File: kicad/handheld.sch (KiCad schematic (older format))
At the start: 30 parts, among them J1 Conn_01x08, J2 61300311121, J3 AVR-PDI-6, SW1 HOLD, SW10 SELECT, SW2 PAUSE, SW3 SDROP, SW4 HDROP, SW5 ROTR, SW6 RIGHT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

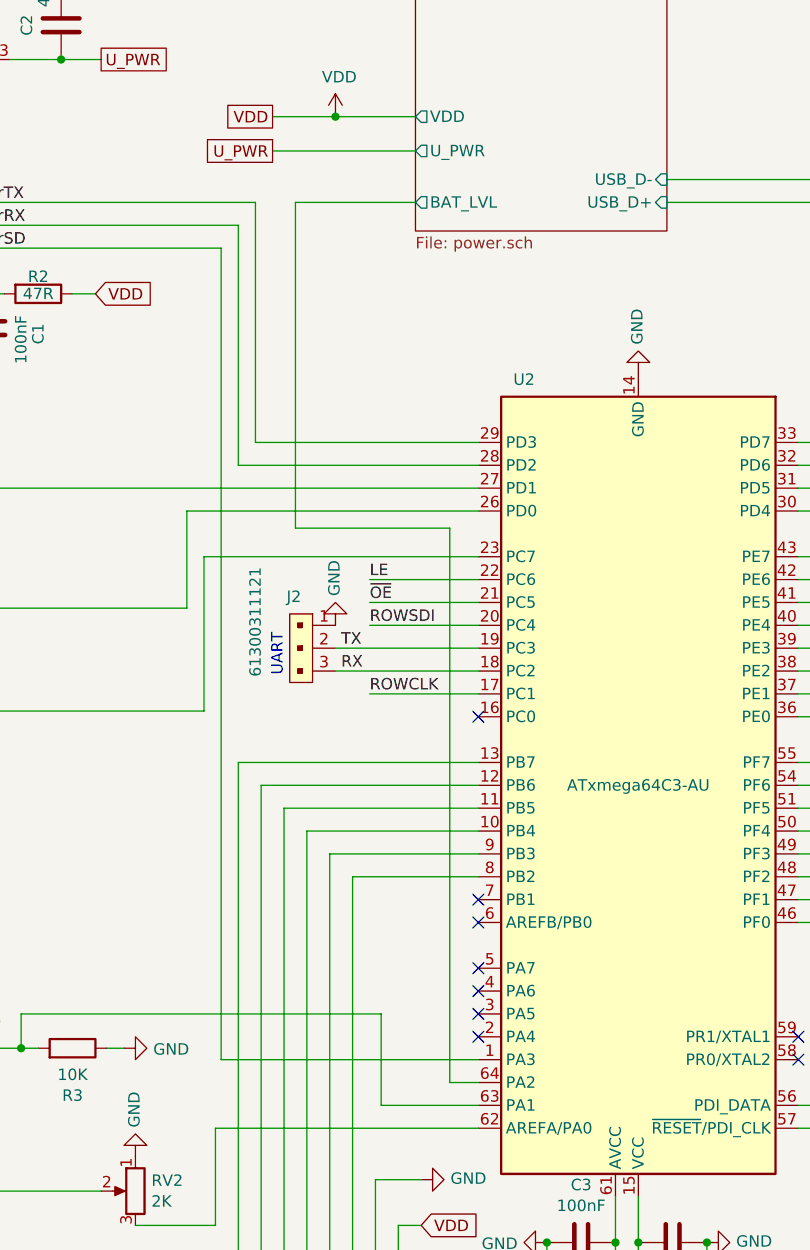
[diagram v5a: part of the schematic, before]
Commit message: Wired up battery level check
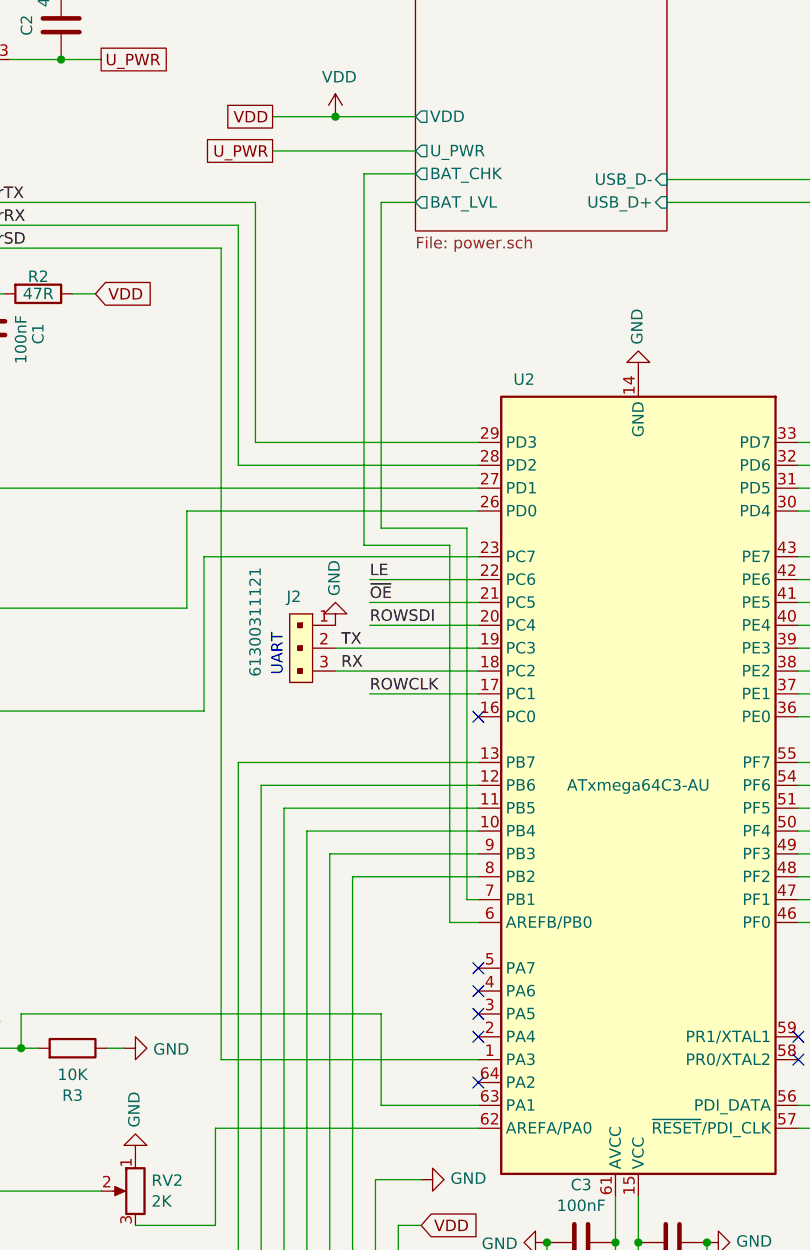
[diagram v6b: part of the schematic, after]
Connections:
- net power/BAT_LVL: now also U2.7 (PB1); no longer U2.64 (PA2)
- net power/BAT_CHK: now reaches U2.6 (AREFB/PB0)
- no-connect marks 9 -> 8
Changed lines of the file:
@@
 F5 "USB_D-" I R 4575 2025 50
 F6 "USB_D+" I R 4575 2125 50
+F7 "BAT_CHK" O L 3475 2000 50
 $EndSheet
 Wire Wire Line
-	3475 2125 2950 2125
-Wire Wire Line
-	3625 5975 3750 5975
+	3475 2125 3325 2125
 Text GLabel 2850 1750 0    50   UnSpc ~ 0
 VDD
@@
 	1925 1500 2100 1500
 Wire Wire Line
-	3625 3550 3625 5975
-Wire Wire Line
-	2950 2125 2950 3550
-Wire Wire Line
-	2950 3550 3625 3550
+	3700 3550 3700 5175
+Wire Wire Line
+	3325 2125 3325 3550
+Wire Wire Line
+	3325 3550 3700 3550
 Text Notes 2750 7075 0    50   ~ 0
 GPIO Expansion
@@
 	1125 4350 2550 4350
 Connection ~ 625  4350
-NoConn ~ 3750 5275
 Wire Wire Line
 	1750 5675 3325 5675
@@
 Wire Wire Line
 	3200 5075 3200 6725
-NoConn ~ 3750 5175
 Wire Wire Line
 	4350 6675 4350 7075
@@
 Wire Wire Line
 	5550 3375 5150 3375
+Wire Wire Line
+	3700 5175 3750 5175
+NoConn ~ 3750 5975
+Wire Wire Line
+	3475 2000 3250 2000
+Wire Wire Line
+	3250 2000 3250 3625
+Wire Wire Line
+	3250 3625 3625 3625
+Wire Wire Line
+	3625 3625 3625 5275
+Wire Wire Line
+	3625 5275 3750 5275
 Wire Bus Line
 	5775 4875 5775 5175

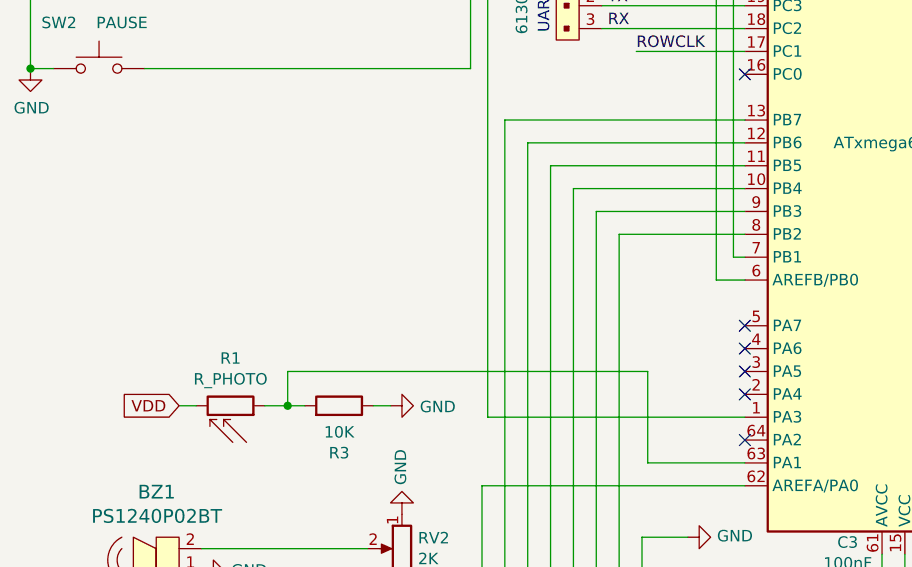
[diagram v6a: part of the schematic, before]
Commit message: Fix register footprints and add batt indicator
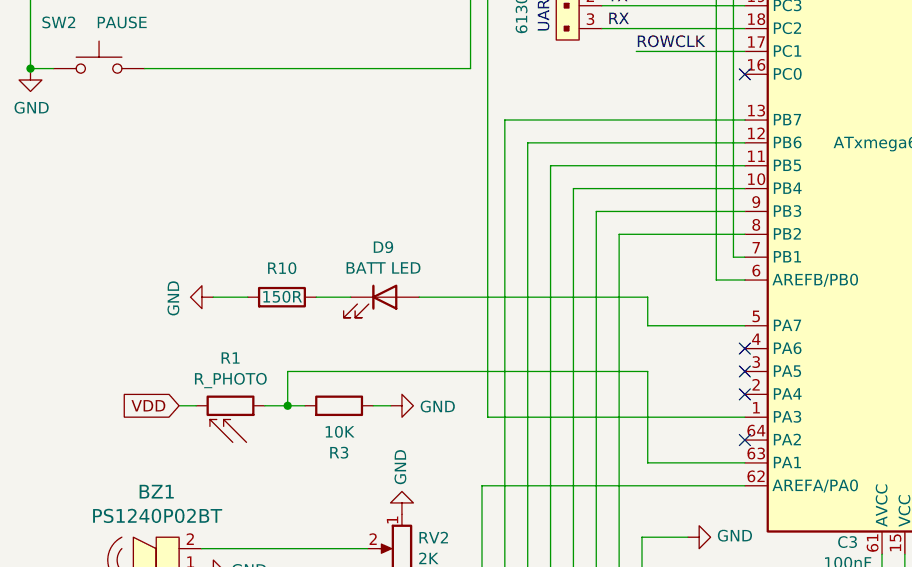
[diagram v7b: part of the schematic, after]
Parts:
- added D9: BATT LED, LED_THT:LED_D3.0mm, symbol Device:LED
- added R10: 150R, Resistor_SMD:R_0805_2012Metric_Pad1.15x1.40mm_HandSolder, symbol Device:R
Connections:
- net GND: now also R10.2
- net at U2.5 (PA7): now also D9.2 (A)
- new net: D9.1 (K), R10.1
- no-connect marks 8 -> 7
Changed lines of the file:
@@
 IrSD
 NoConn ~ 3750 4375
-NoConn ~ 3750 5475
 NoConn ~ 3750 5575
 NoConn ~ 3750 5675
@@
 Wire Wire Line
 	3625 5275 3750 5275
+$Comp
+L Device:LED D9
+U 1 1 5FE05E08
+P 2175 5350
+F 0 "D9" H 2168 5567 50  0000 C CNN
+F 1 "BATT LED" H 2168 5476 50  0000 C CNN
+F 2 "LED_THT:LED_D3.0mm" H 2175 5350 50  0001 C CNN
+F 3 "~" H 2175 5350 50  0001 C CNN
+	1    2175 5350
+	1    0    0    -1
+$EndComp
+Wire Wire Line
+	2325 5350 3325 5350
+Wire Wire Line
+	3325 5350 3325 5475
+Wire Wire Line
+	3325 5475 3750 5475
+$Comp
+L Device:R R10
+U 1 1 5FE0E9B8
+P 1725 5350
+F 0 "R10" V 1850 5350 50  0000 C CNN
+F 1 "150R" V 1725 5350 50  0000 C CNN
+F 2 "Resistor_SMD:R_0805_2012Metric_Pad1.15x1.40mm_HandSolder" V 1655 5350 50  0001 C CNN
+F 3 "~" H 1725 5350 50  0001 C CNN
+	1    1725 5350
+	0    1    -1   0
+$EndComp
+Wire Wire Line
+	1875 5350 2025 5350
+$Comp
+L power:GND #PWR0102
+U 1 1 5FE1738F
+P 1425 5350
+F 0 "#PWR0102" H 1425 5100 50  0001 C CNN
+F 1 "GND" H 1430 5177 50  0000 C CNN
+F 2 "" H 1425 5350 50  0001 C CNN
+F 3 "" H 1425 5350 50  0001 C CNN
+	1    1425 5350
+	0    1    1    0
+$EndComp
+Wire Wire Line
+	1425 5350 1575 5350
 Wire Bus Line
 	5775 4875 5775 5175

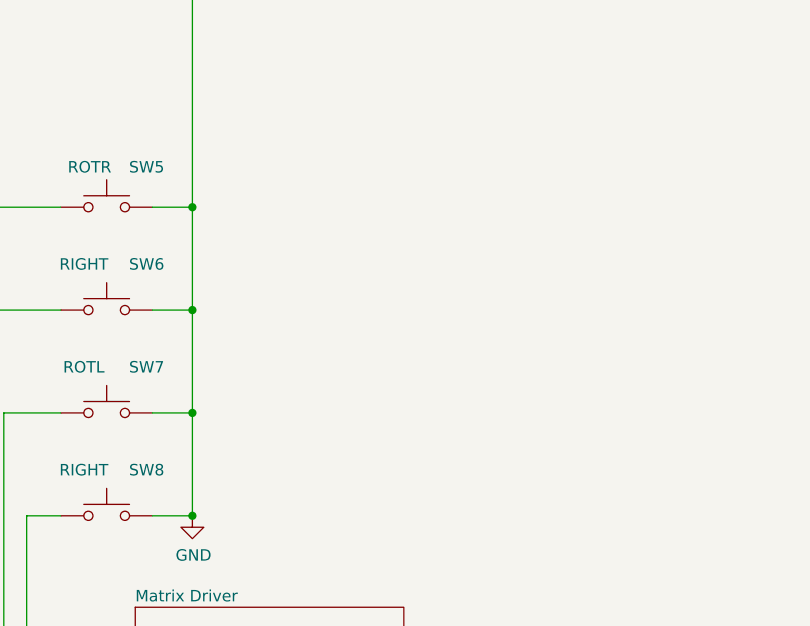
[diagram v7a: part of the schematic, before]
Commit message: Switched to registers with clear
Also added the mountng holes as annotated symbols with footprints.
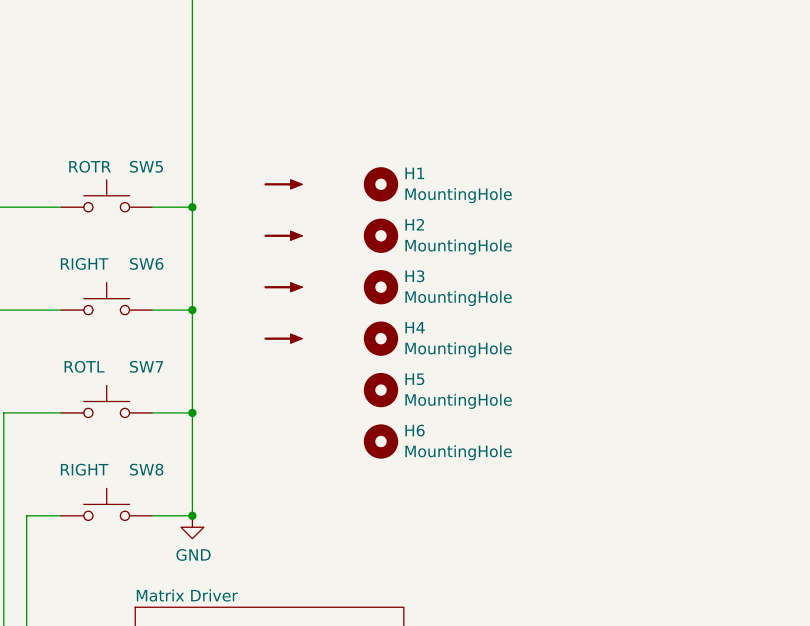
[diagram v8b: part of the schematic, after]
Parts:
- added H1, H2, H3, H4, H5, H6: MountingHole, MountingHole:MountingHole_3.2mm_M3, symbol Mechanical:MountingHole
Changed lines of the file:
@@
 Wire Bus Line
 	5775 4475 5775 4875
+$Comp
+L Mechanical:MountingHole H1
+U 1 1 5FE0E6C0
+P 8625 2000
+F 0 "H1" H 8725 2046 50  0000 L CNN
+F 1 "MountingHole" H 8725 1955 50  0000 L CNN
+F 2 "MountingHole:MountingHole_3.2mm_M3" H 8625 2000 50  0001 C CNN
+F 3 "~" H 8625 2000 50  0001 C CNN
+	1    8625 2000
+	1    0    0    -1
+$EndComp
+$Comp
+L Mechanical:MountingHole H2
+U 1 1 5FE0E95C
+P 8625 2225
+F 0 "H2" H 8725 2271 50  0000 L CNN
+F 1 "MountingHole" H 8725 2180 50  0000 L CNN
+F 2 "MountingHole:MountingHole_3.2mm_M3" H 8625 2225 50  0001 C CNN
+F 3 "~" H 8625 2225 50  0001 C CNN
+	1    8625 2225
+	1    0    0    -1
+$EndComp
+$Comp
+L Mechanical:MountingHole H3
+U 1 1 5FE0F471
+P 8625 2450
+F 0 "H3" H 8725 2496 50  0000 L CNN
+F 1 "MountingHole" H 8725 2405 50  0000 L CNN
+F 2 "MountingHole:MountingHole_3.2mm_M3" H 8625 2450 50  0001 C CNN
+F 3 "~" H 8625 2450 50  0001 C CNN
+	1    8625 2450
+	1    0    0    -1
+$EndComp
+$Comp
+L Mechanical:MountingHole H4
+U 1 1 5FE0F840
+P 8625 2675
+F 0 "H4" H 8725 2721 50  0000 L CNN
+F 1 "MountingHole" H 8725 2630 50  0000 L CNN
+F 2 "MountingHole:MountingHole_3.2mm_M3" H 8625 2675 50  0001 C CNN
+F 3 "~" H 8625 2675 50  0001 C CNN
+	1    8625 2675
+	1    0    0    -1
+$EndComp
+$Comp
+L Mechanical:MountingHole H5
+U 1 1 5FE0FBDC
+P 8625 2900
+F 0 "H5" H 8725 2946 50  0000 L CNN
+F 1 "MountingHole" H 8725 2855 50  0000 L CNN
+F 2 "MountingHole:MountingHole_3.2mm_M3" H 8625 2900 50  0001 C CNN
+F 3 "~" H 8625 2900 50  0001 C CNN
+	1    8625 2900
+	1    0    0    -1
+$EndComp
+$Comp
+L Mechanical:MountingHole H6
+U 1 1 5FE0FE57
+P 8625 3125
+F 0 "H6" H 8725 3171 50  0000 L CNN
+F 1 "MountingHole" H 8725 3080 50  0000 L CNN
+F 2 "MountingHole:MountingHole_3.2mm_M3" H 8625 3125 50  0001 C CNN
+F 3 "~" H 8625 3125 50  0001 C CNN
+	1    8625 3125
+	1    0    0    -1
+$EndComp
+$Comp
+L Graphic:SYM_Arrow_Small #SYM1
+U 1 1 5FE18196
+P 8200 2000
+F 0 "#SYM1" H 8200 2060 50  0001 C CNN
+F 1 "SYM_Arrow_Small" H 8210 1950 50  0001 C CNN
+F 2 "arrow:arraw_6mm" H 8200 2000 50  0001 C CNN
+F 3 "~" H 8200 2000 50  0001 C CNN
+	1    8200 2000
+	1    0    0    -1
+$EndComp
+$Comp
+L Graphic:SYM_Arrow_Small #SYM2
+U 1 1 5FE18F35
+P 8200 2225
+F 0 "#SYM2" H 8200 2285 50  0001 C CNN
+F 1 "SYM_Arrow_Small" H 8210 2175 50  0001 C CNN
+F 2 "arrow:arraw_6mm" H 8200 2225 50  0001 C CNN
+F 3 "~" H 8200 2225 50  0001 C CNN
+	1    8200 2225
+	1    0    0    -1
+$EndComp
+$Comp
+L Graphic:SYM_Arrow_Small #SYM3
+U 1 1 5FE1929E
+P 8200 2450
+F 0 "#SYM3" H 8200 2510 50  0001 C CNN
+F 1 "SYM_Arrow_Small" H 8210 2400 50  0001 C CNN
+F 2 "arrow:arraw_6mm" H 8200 2450 50  0001 C CNN
+F 3 "~" H 8200 2450 50  0001 C CNN
+	1    8200 2450
+	1    0    0    -1
+$EndComp
+$Comp
+L Graphic:SYM_Arrow_Small #SYM4
+U 1 1 5FE194F7
+P 8200 2675
+F 0 "#SYM4" H 8200 2735 50  0001 C CNN
+F 1 "SYM_Arrow_Small" H 8210 2625 50  0001 C CNN
+F 2 "arrow:arraw_6mm" H 8200 2675 50  0001 C CNN
+F 3 "~" H 8200 2675 50  0001 C CNN
+	1    8200 2675
+	1    0    0    -1
+$EndComp
 $EndSCHEMATC
